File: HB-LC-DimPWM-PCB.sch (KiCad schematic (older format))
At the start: 74 parts, among them J1 SWD, J2 12V Input, J3 Conn_01x04_Male, Q1 S9013, Q10 BSS84, Q11 2N7002, Q12 BSS84, Q13 2N7002, Q14 VS5810AS, Q15 VS5810AS, Q16 VS5810AS, Q2 BSS84, Q3 2N7002, Q4 VS5810AS, Q5 S9013, Q6 S9013, Q7 S9013, Q8 BSS84, Q9 2N7002, U1 STM32F103C8Tx, U2 AMS1117-3.3, Y1 8MHz

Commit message: Add alternate gate driver setup
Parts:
- added C25, C26, C27, C28, C41, C42, C43, C44, C45, C46, C47, C48: 1uF, Capacitor_SMD:C_0402_1005Metric, symbol Device:C
- added C29, C30, C31, C32, C49, C50, C51, C52, C53, C54, C55, C56: 100n, Capacitor_SMD:C_0603_1608Metric, symbol Device:C
- added C33, C34, C35, C36, C57, C58, C59, C60, C61, C62, C63, C64: 100p, Capacitor_SMD:C_0402_1005Metric, symbol Device:C
- added C37, C38, C39, C40, C65, C66, C67, C68, C69, C70, C71, C72: 1uF, Capacitor_SMD:C_0603_1608Metric, symbol Device:C
- added F10, F11, F12, F13, F14, F15, F16, F17, F6, F7, F8, F9: 15V 5A, Fuse:Fuse_2920_7451Metric, symbol Device:Polyfuse
- added J4, J5, J6: Conn_01x04_Male, Connector_Phoenix_MC_HighVoltage:PhoenixContact_MC_1,5_4-G-5.08_1x04_P5.08mm_Horizontal, symbol Connector:Conn_01x04_Male
- added L10, L11, L12, L13, L14, L15, L16, L5, L6, L7, L8, L9: 3.3uH, Inductor_Sunlord:SMD-PIND-10.5x11.5x4_2.5x3.0, symbol Device:L
- added Q17, Q18, Q19, Q20, Q21, Q22, Q23, Q24, Q25, Q26, Q27, Q28: VS5810AS, Package_SO:SOIC-8_3.9x4.9mm_P1.27mm, symbol Transistor_FET:FDS6630A
- added R20, R21, R22, R23, R24, R25, R26, R27, R28, R29, R30, R31: 10k, Resistor_SMD:R_0402_1005Metric, symbol Device:R
- added U10, U11, U12, U13, U14, U3, U4, U5, U6, U7, U8, U9: MCP1416, Package_TO_SOT_SMD:SOT-23-5, symbol Driver_FET:MCP1416
- R14, R15, R16, R17, R18, R19, R6, R7: footprint Resistor_SMD:R_0805_2012Metric -> Resistor_SMD:R_0603_1608Metric; LCSC C17561 -> C23345
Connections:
- wire segments 164 -> 530
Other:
- moved on the sheet: C13, C14, C15, C16, C17, C18, C19, C20, C21, C22, C23, C24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

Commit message: Layout one dimmer channel
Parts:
- removed C25, C26, C27, C28, C41, C42, C43, C44, C45, C46, C47, C48: 1uF, Capacitor_SMD:C_0402_1005Metric, symbol Device:C
- removed C29, C30, C31, C32, C49, C50, C51, C52, C53, C54, C55, C56: 100n, Capacitor_SMD:C_0603_1608Metric, symbol Device:C
- removed C33, C34, C35, C36, C57, C58, C59, C60, C61, C62, C63, C64: 100p, Capacitor_SMD:C_0402_1005Metric, symbol Device:C
- removed C37, C38, C39, C40, C65, C66, C67, C68, C69, C70, C71, C72: 1uF, Capacitor_SMD:C_0603_1608Metric, symbol Device:C
- removed F10, F11, F12, F13, F14, F15, F16, F17, F6, F7, F8, F9: 15V 5A, Fuse:Fuse_2920_7451Metric, symbol Device:Polyfuse
- removed J4, J5, J6: Conn_01x04_Male, Connector_Phoenix_MC_HighVoltage:PhoenixContact_MC_1,5_4-G-5.08_1x04_P5.08mm_Horizontal, symbol Connector:Conn_01x04_Male
- removed L10, L11, L12, L13, L14, L15, L16, L5, L6, L7, L8, L9: 3.3uH, Inductor_Sunlord:SMD-PIND-10.5x11.5x4_2.5x3.0, symbol Device:L
- removed Q17, Q18, Q19, Q20, Q21, Q22, Q23, Q24, Q25, Q26, Q27, Q28: VS5810AS, Package_SO:SOIC-8_3.9x4.9mm_P1.27mm, symbol Transistor_FET:FDS6630A
- removed R20, R21, R22, R23, R24, R25, R26, R27, R28, R29, R30, R31: 10k, Resistor_SMD:R_0402_1005Metric, symbol Device:R
- removed U10, U11, U12, U13, U14, U3, U4, U5, U6, U7, U8, U9: MCP1416, Package_TO_SOT_SMD:SOT-23-5, symbol Driver_FET:MCP1416
- C17, C18, C19, C20: footprint Capacitor_SMD:C_0402_1005Metric -> Capacitor_SMD:C_0805_2012Metric; LCSC C1546 -> C1790
- C21, C22, C23: footprint Capacitor_SMD:C_0603_1608Metric -> Capacitor_SMD:C_1206_3216Metric; LCSC C15849 -> C1848
- C24: footprint Capacitor_SMD:C_0603_1608Metric -> Capacitor_SMD:C_1206_3216Metric
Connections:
- wire segments 530 -> 164

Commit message: Add full layout as PoC
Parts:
- added C25, C26, C27, C28, C37, C38, C39, C40, C41, C42, C43, C44: 1uF, Capacitor_SMD:C_0402_1005Metric, symbol Device:C
- added C29, C30, C31, C32, C45, C46, C47, C48, C49, C50, C51, C52: 100p, Capacitor_SMD:C_0805_2012Metric, symbol Device:C
- added C33, C34, C35, C36, C53, C54, C55, C56, C57, C58, C59, C60: 1uF, Capacitor_SMD:C_1206_3216Metric, symbol Device:C
- added F10, F11, F12, F13, F14, F15, F16, F17, F6, F7, F8, F9: 15V 5A, Fuse:Fuse_2920_7451Metric, symbol Device:Polyfuse
- added J4, J5, J6: Conn_01x04_Male, Connector_Phoenix_MC_HighVoltage:PhoenixContact_MC_1,5_4-G-5.08_1x04_P5.08mm_Horizontal, symbol Connector:Conn_01x04_Male
- added L10, L11, L12, L13, L14, L15, L16, L5, L6, L7, L8, L9: 3.3uH, Inductor_Sunlord:SMD-PIND-10.5x11.5x4_2.5x3.0, symbol Device:L
- added Q17, Q18, Q19, Q20, Q33, Q34, Q35, Q36, Q37, Q38, Q39, Q40: S9013, Package_TO_SOT_SMD:SOT-23, symbol Device:Q_NPN_BEC
- added Q21, Q23, Q25, Q27, Q41, Q43, Q45, Q47, Q49, Q51, Q53, Q55: BSS84, Package_TO_SOT_SMD:SOT-23, symbol Transistor_FET:BSS84
- added Q22, Q24, Q26, Q28, Q42, Q44, Q46, Q48, Q50, Q52, Q54, Q56: 2N7002, Package_TO_SOT_SMD:SOT-23, symbol Transistor_FET:2N7002
- added Q29, Q30, Q31, Q32, Q57, Q58, Q59, Q60, Q61, Q62, Q63, Q64: VS5810AS, Package_SO:SOIC-8_3.9x4.9mm_P1.27mm, symbol Transistor_FET:FDS6630A
- added R20, R21, R22, R23, R36, R37, R38, R39, R40, R41, R42, R43: 10k, Resistor_SMD:R_0402_1005Metric, symbol Device:R
- added R24, R25, R26, R27, R44, R45, R46, R47, R48, R49, R50, R51: 1k, Resistor_SMD:R_0402_1005Metric, symbol Device:R
- added R28, R29, R30, R31, R32, R33, R34, R35, R52, R53, R54, R55, R56, R57, R58, R59, R60, R61, R62, R63, R64, R65, R66, R67: 22R, Resistor_SMD:R_0603_1608Metric, symbol Device:R
- added U3: HomeMatic-sensor, HomeMatic-sensor:HomeMatic-sensor, symbol HomeMatic-sensor:HomeMatic-sensor
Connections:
- net +12V: now also C25.1, C26.1, C27.1, C28.1, C37.1, C38.1, C39.1, C40.1, C41.1, C42.1, C43.1, C44.1, Q21.2 (S), Q23.2 (S), Q25.2 (S), Q27.2 (S), Q41.2 (S), Q43.2 (S), Q45.2 (S), Q47.2 (S), Q49.2 (S), Q51.2 (S), Q53.2 (S), Q55.2 (S), R24.2, R25.2, R26.2, R27.2, R44.2, R45.2, R46.2, R47.2, R48.2, R49.2, R50.2, R51.2
- net GND: now also C25.2, C26.2, C27.2, C28.2, C29.2, C30.2, C31.2, C32.2, C33.2, C34.2, C35.2, C36.2, C37.2, C38.2, C39.2, C40.2, C41.2, C42.2, C43.2, C44.2, C45.2, C46.2, C47.2, C48.2, C49.2, C50.2, C51.2, C52.2, C53.2, C54.2, C55.2, C56.2, C57.2, C58.2, C59.2, C60.2, Q17.2 (E), Q18.2 (E), Q19.2 (E), Q20.2 (E), Q22.2 (S), Q24.2 (S), Q26.2 (S), Q28.2 (S), Q29.1 (S), Q29.2 (S), Q29.3 (S), Q30.1 (S), Q30.2 (S), Q30.3 (S), Q31.1 (S), Q31.2 (S), Q31.3 (S), Q32.1 (S), Q32.2 (S), Q32.3 (S), Q33.2 (E), Q34.2 (E), Q35.2 (E), Q36.2 (E), Q37.2 (E), Q38.2 (E), Q39.2 (E), Q40.2 (E), Q42.2 (S), Q44.2 (S), Q46.2 (S), Q48.2 (S), Q50.2 (S), Q52.2 (S), Q54.2 (S), Q56.2 (S), Q57.1 (S), Q57.2 (S), Q57.3 (S), Q58.1 (S), Q58.2 (S), Q58.3 (S), Q59.1 (S), Q59.2 (S), Q59.3 (S), Q60.1 (S), Q60.2 (S), Q60.3 (S), Q61.1 (S), Q61.2 (S), Q61.3 (S), Q62.1 (S), Q62.2 (S), Q62.3 (S), Q63.1 (S), Q63.2 (S), Q63.3 (S), Q64.1 (S), Q64.2 (S), Q64.3 (S)
- new net: F10.1, J5.1 (Pin_1)
- new net: F11.1, J5.2 (Pin_2)
- new net: F12.1, J5.3 (Pin_3)
- new net: F13.1, J5.4 (Pin_4)
- new net: C53.1, F10.2, L9.2
- new net: C45.1, L9.1, Q57.5 (D), Q57.6 (D), Q57.7 (D), Q57.8 (D)
- new net: Q57.4 (G), R52.2, R53.1
- new net: Q42.3 (D), R53.2
- new net: Q41.3 (D), R52.1
- new net: Q33.3 (C), Q41.1 (G), Q42.1 (G), R44.1
- new net: Q33.1 (B), R36.2
- new net: C54.1, F11.2, L10.2
- new net: C46.1, L10.1, Q58.5 (D), Q58.6 (D), Q58.7 (D), Q58.8 (D)
- new net: Q58.4 (G), R54.2, R55.1
- new net: Q44.3 (D), R55.2
- new net: Q43.3 (D), R54.1
- new net: Q34.3 (C), Q43.1 (G), Q44.1 (G), R45.1
- new net: Q34.1 (B), R37.2
- new net: C55.1, F12.2, L11.2
- new net: C47.1, L11.1, Q59.5 (D), Q59.6 (D), Q59.7 (D), Q59.8 (D)
- new net: Q59.4 (G), R56.2, R57.1
- new net: Q46.3 (D), R57.2
- new net: Q45.3 (D), R56.1
- new net: Q35.3 (C), Q45.1 (G), Q46.1 (G), R46.1
- new net: Q35.1 (B), R38.2
- new net: C56.1, F13.2, L12.2
- new net: C48.1, L12.1, Q60.5 (D), Q60.6 (D), Q60.7 (D), Q60.8 (D)
- new net: Q60.4 (G), R58.2, R59.1
- new net: Q48.3 (D), R59.2
- new net: Q47.3 (D), R58.1
- new net: Q36.3 (C), Q47.1 (G), Q48.1 (G), R47.1
- new net: Q36.1 (B), R39.2
- new net: F6.1, J4.1 (Pin_1)
- new net: F7.1, J4.2 (Pin_2)
- new net: F8.1, J4.3 (Pin_3)
- new net: F9.1, J4.4 (Pin_4)
- new net: C33.1, F6.2, L5.2
- new net: C29.1, L5.1, Q29.5 (D), Q29.6 (D), Q29.7 (D), Q29.8 (D)
- new net: Q29.4 (G), R28.2, R29.1
- new net: Q22.3 (D), R29.2
- new net: Q21.3 (D), R28.1
- new net: Q17.3 (C), Q21.1 (G), Q22.1 (G), R24.1
- new net: Q17.1 (B), R20.2
- new net: C34.1, F7.2, L6.2
- new net: C30.1, L6.1, Q30.5 (D), Q30.6 (D), Q30.7 (D), Q30.8 (D)
- new net: Q30.4 (G), R30.2, R31.1
- new net: Q24.3 (D), R31.2
- new net: Q23.3 (D), R30.1
- new net: Q18.3 (C), Q23.1 (G), Q24.1 (G), R25.1
- new net: Q18.1 (B), R21.2
- new net: C35.1, F8.2, L7.2
- new net: C31.1, L7.1, Q31.5 (D), Q31.6 (D), Q31.7 (D), Q31.8 (D)
- new net: Q31.4 (G), R32.2, R33.1
- new net: Q26.3 (D), R33.2
- new net: Q25.3 (D), R32.1
- new net: Q19.3 (C), Q25.1 (G), Q26.1 (G), R26.1
- new net: Q19.1 (B), R22.2
- new net: C36.1, F9.2, L8.2
- new net: C32.1, L8.1, Q32.5 (D), Q32.6 (D), Q32.7 (D), Q32.8 (D)
- new net: Q32.4 (G), R34.2, R35.1
- new net: Q28.3 (D), R35.2
- new net: Q27.3 (D), R34.1
- new net: Q20.3 (C), Q27.1 (G), Q28.1 (G), R27.1
- new net: Q20.1 (B), R23.2
- new net: F14.1, J6.1 (Pin_1)
- new net: F15.1, J6.2 (Pin_2)
- new net: F16.1, J6.3 (Pin_3)
- new net: F17.1, J6.4 (Pin_4)
- new net: C57.1, F14.2, L13.2
- new net: C49.1, L13.1, Q61.5 (D), Q61.6 (D), Q61.7 (D), Q61.8 (D)
- new net: Q61.4 (G), R60.2, R61.1
- new net: Q50.3 (D), R61.2
- new net: Q49.3 (D), R60.1
- new net: Q37.3 (C), Q49.1 (G), Q50.1 (G), R48.1
- new net: Q37.1 (B), R40.2
- new net: C58.1, F15.2, L14.2
- new net: C50.1, L14.1, Q62.5 (D), Q62.6 (D), Q62.7 (D), Q62.8 (D)
- new net: Q62.4 (G), R62.2, R63.1
- new net: Q52.3 (D), R63.2
- new net: Q51.3 (D), R62.1
- new net: Q38.3 (C), Q51.1 (G), Q52.1 (G), R49.1
- new net: Q38.1 (B), R41.2
- new net: C59.1, F16.2, L15.2
- new net: C51.1, L15.1, Q63.5 (D), Q63.6 (D), Q63.7 (D), Q63.8 (D)
- new net: Q63.4 (G), R64.2, R65.1
- new net: Q54.3 (D), R65.2
- new net: Q53.3 (D), R64.1
- new net: Q39.3 (C), Q53.1 (G), Q54.1 (G), R50.1
- new net: Q39.1 (B), R42.2
- new net: C60.1, F17.2, L16.2
- new net: C52.1, L16.1, Q64.5 (D), Q64.6 (D), Q64.7 (D), Q64.8 (D)
- new net: Q64.4 (G), R66.2, R67.1
- new net: Q56.3 (D), R67.2
- new net: Q55.3 (D), R66.1
- new net: Q40.3 (C), Q55.1 (G), Q56.1 (G), R51.1
- new net: Q40.1 (B), R43.2
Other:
- moved on the sheet: C13, C14, C15, C16, C17, C18, C19, C20, C21, C22, C23, C24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

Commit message: Use hierarchical sheet for dimmer channels
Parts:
- removed C13, C14, C15, C16, C25, C26, C27, C28, C37, C38, C39, C40, C41, C42, C43, C44: 1uF, Capacitor_SMD:C_0402_1005Metric, symbol Device:C
- removed C17, C18, C19, C20, C29, C30, C31, C32, C45, C46, C47, C48, C49, C50, C51, C52: 100p, Capacitor_SMD:C_0805_2012Metric, symbol Device:C
- removed C21, C22, C23, C24, C33, C34, C35, C36, C53, C54, C55, C56, C57, C58, C59, C60: 1uF, Capacitor_SMD:C_1206_3216Metric, symbol Device:C
- removed F10, F11, F12, F13, F14, F15, F16, F17, F2, F3, F4, F5, F6, F7, F8, F9: 15V 5A, Fuse:Fuse_2920_7451Metric, symbol Device:Polyfuse
- removed J3, J4, J5, J6: Conn_01x04_Male, Connector_Phoenix_MC_HighVoltage:PhoenixContact_MC_1,5_4-G-5.08_1x04_P5.08mm_Horizontal, symbol Connector:Conn_01x04_Male
- removed L1, L10, L11, L12, L13, L14, L15, L16, L2, L3, L4, L5, L6, L7, L8, L9: 3.3uH, Inductor_Sunlord:SMD-PIND-10.5x11.5x4_2.5x3.0, symbol Device:L
- removed Q1, Q17, Q18, Q19, Q20, Q33, Q34, Q35, Q36, Q37, Q38, Q39, Q40, Q5, Q6, Q7: S9013, Package_TO_SOT_SMD:SOT-23, symbol Device:Q_NPN_BEC
- removed Q10, Q12, Q2, Q21, Q23, Q25, Q27, Q41, Q43, Q45, Q47, Q49, Q51, Q53, Q55, Q8: BSS84, Package_TO_SOT_SMD:SOT-23, symbol Transistor_FET:BSS84
- removed Q11, Q13, Q22, Q24, Q26, Q28, Q3, Q42, Q44, Q46, Q48, Q50, Q52, Q54, Q56, Q9: 2N7002, Package_TO_SOT_SMD:SOT-23, symbol Transistor_FET:2N7002
- removed Q14, Q15, Q16, Q29, Q30, Q31, Q32, Q4, Q57, Q58, Q59, Q60, Q61, Q62, Q63, Q64: VS5810AS, Package_SO:SOIC-8_3.9x4.9mm_P1.27mm, symbol Transistor_FET:FDS6630A
- removed R10, R20, R21, R22, R23, R36, R37, R38, R39, R4, R40, R41, R42, R43, R8, R9: 10k, Resistor_SMD:R_0402_1005Metric, symbol Device:R
- removed R11, R12, R13, R24, R25, R26, R27, R44, R45, R46, R47, R48, R49, R5, R50, R51: 1k, Resistor_SMD:R_0402_1005Metric, symbol Device:R
- removed R14, R15, R16, R17, R18, R19, R28, R29, R30, R31, R32, R33, R34, R35, R52, R53, R54, R55, R56, R57, R58, R59, R6, R60, R61, R62, R63, R64, R65, R66, R67, R7: 22R, Resistor_SMD:R_0603_1608Metric, symbol Device:R

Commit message: First eight channels finished
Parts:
- added D?: D_Schottky, symbol Device:D_Schottky
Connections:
- net +3V3: now also U3.8 (VDD)
- net GND: now also U3.2 (GND)
- net ~RST: now reaches C1.1, R1.2, U1.7 (NRST)
- net ~RST: now also D?.2 (A)
- net SDA: now reaches U3.3 (SDA)
- net SCL: now reaches U3.4 (SCL)
- net at U3.7 (GPIO): now also D?.1 (K)
- no-connect marks 7 -> 8
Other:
- moved on the sheet: U3
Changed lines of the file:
@@
 	1    0    0    -1
 $EndComp
-Text Label 3750 5050 0    50   ~ 0
+Text Label 4100 5050 2    50   ~ 0
 SWCLK
-Text Label 3750 4950 0    50   ~ 0
+Text Label 4100 4950 2    50   ~ 0
 SWDIO
 NoConn ~ 2450 3450
@@
 L HomeMatic-sensor:HomeMatic-sensor U3
 U 1 1 5E9FF214
-P 5900 8150
-F 0 "U3" H 5900 9131 50  0000 C CNN
-F 1 "HomeMatic-sensor" H 5900 9040 50  0000 C CNN
-F 2 "HomeMatic-sensor:HomeMatic-sensor" H 5900 8150 50  0001 C CNN
-F 3 "" H 5900 8150 50  0001 C CNN
-	1    5900 8150
+P 2050 7200
+F 0 "U3" H 1600 7950 50  0000 C CNN
+F 1 "HomeMatic-sensor" H 2450 7950 50  0000 C CNN
+F 2 "HomeMatic-sensor:HomeMatic-sensor" H 2050 7200 50  0001 C CNN
+F 3 "" H 2050 7200 50  0001 C CNN
+	1    2050 7200
 	1    0    0    -1
 $EndComp
@@
 Wire Wire Line
 	8550 8600 8550 8750
+Text Label 2150 2200 0    50   ~ 0
+~RST
+Wire Wire Line
+	4100 4950 3750 4950
+Wire Wire Line
+	4100 5050 3750 5050
+$Comp
+L power:+3V3 #PWR?
+U 1 1 5EC451F2
+P 2050 6300
+F 0 "#PWR?" H 2050 6150 50  0001 C CNN
+F 1 "+3V3" H 2065 6473 50  0000 C CNN
+F 2 "" H 2050 6300 50  0001 C CNN
+F 3 "" H 2050 6300 50  0001 C CNN
+	1    2050 6300
+	1    0    0    -1
+$EndComp
+Wire Wire Line
+	2050 6300 2050 6400
+$Comp
+L power:GND #PWR?
+U 1 1 5EC474BA
+P 2050 8000
+F 0 "#PWR?" H 2050 7750 50  0001 C CNN
+F 1 "GND" H 2055 7827 50  0000 C CNN
+F 2 "" H 2050 8000 50  0001 C CNN
+F 3 "" H 2050 8000 50  0001 C CNN
+	1    2050 8000
+	1    0    0    -1
+$EndComp
+Wire Wire Line
+	2050 8000 2050 7900
+$Comp
+L Device:D_Schottky D?
+U 1 1 5EC49805
+P 3000 7050
+F 0 "D?" H 3000 7266 50  0000 C CNN
+F 1 "D_Schottky" H 3000 7175 50  0000 C CNN
+F 2 "" H 3000 7050 50  0001 C CNN
+F 3 "~" H 3000 7050 50  0001 C CNN
+	1    3000 7050
+	1    0    0    -1
+$EndComp
+NoConn ~ 2700 6900
+Text Label 3400 7050 2    50   ~ 0
+~RST
+Wire Wire Line
+	3400 7050 3150 7050
+Wire Wire Line
+	2850 7050 2700 7050
+Text Label 1150 6900 0    50   ~ 0
+SDA
+Wire Wire Line
+	1150 6900 1400 6900
+Text Label 1150 7050 0    50   ~ 0
+SCL
+Wire Wire Line
+	1150 7050 1400 7050
 $EndSCHEMATC

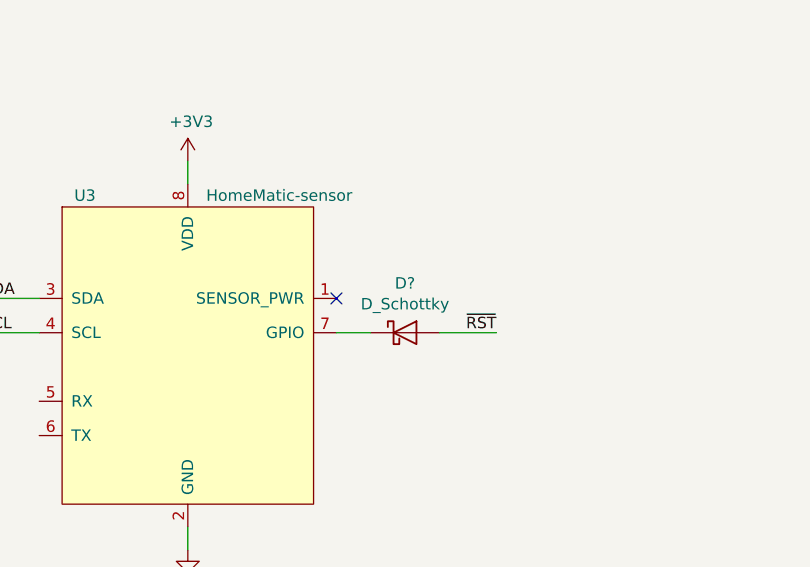
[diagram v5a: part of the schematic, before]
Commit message: Replace 5.08 mm pitch headers by 3.5 mm pitch
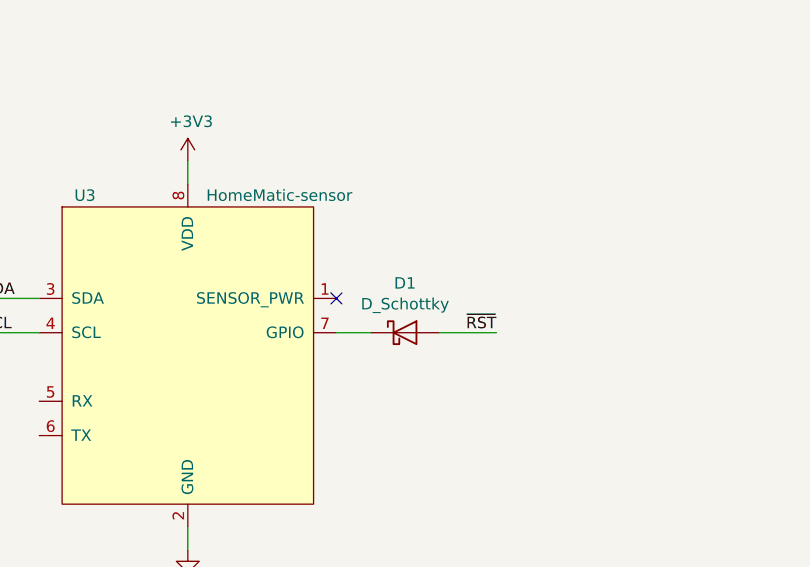
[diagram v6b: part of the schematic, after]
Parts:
- J2: footprint (none) -> Connector_Phoenix_MC_HighVoltage:PhoenixContact_MC_1,5_2-G-5.08_1x02_P5.08mm_Horizontal
- gave numbers to parts that had none: 1
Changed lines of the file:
@@
 F 0 "J2" H 1058 1231 50  0000 C CNN
 F 1 "12V Input" H 1058 1140 50  0000 C CNN
-F 2 "" H 950 1050 50  0001 C CNN
+F 2 "Connector_Phoenix_MC_HighVoltage:PhoenixContact_MC_1,5_2-G-5.08_1x02_P5.08mm_Horizontal" H 950 1050 50  0001 C CNN
 F 3 "~" H 950 1050 50  0001 C CNN
 	1    950  1050
@@
 	4100 5050 3750 5050
 $Comp
-L power:+3V3 #PWR?
+L power:+3V3 #PWR0121
 U 1 1 5EC451F2
 P 2050 6300
-F 0 "#PWR?" H 2050 6150 50  0001 C CNN
+F 0 "#PWR0121" H 2050 6150 50  0001 C CNN
 F 1 "+3V3" H 2065 6473 50  0000 C CNN
 F 2 "" H 2050 6300 50  0001 C CNN
@@
 	2050 6300 2050 6400
 $Comp
-L power:GND #PWR?
+L power:GND #PWR0122
 U 1 1 5EC474BA
 P 2050 8000
-F 0 "#PWR?" H 2050 7750 50  0001 C CNN
+F 0 "#PWR0122" H 2050 7750 50  0001 C CNN
 F 1 "GND" H 2055 7827 50  0000 C CNN
 F 2 "" H 2050 8000 50  0001 C CNN
@@
 	2050 8000 2050 7900
 $Comp
-L Device:D_Schottky D?
+L Device:D_Schottky D1
 U 1 1 5EC49805
 P 3000 7050
-F 0 "D?" H 3000 7266 50  0000 C CNN
+F 0 "D1" H 3000 7266 50  0000 C CNN
 F 1 "D_Schottky" H 3000 7175 50  0000 C CNN
 F 2 "" H 3000 7050 50  0001 C CNN

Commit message: Layout board
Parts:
- added F18, F19: 500mA, Fuse:Fuse_2512_6332Metric, symbol Device:Fuse
- D1: footprint (none) -> Diode_SMD:D_SOD-123; LCSC (none) -> C8598
- J2: footprint Connector_Phoenix_MC_HighVoltage:PhoenixContact_MC_1,5_2-G-5.08_1x02_P5.08mm_Horizontal -> Connector_Wago_714:Wago_714-162_1x02_P3.50mm_Horizontal
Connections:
- net +12V: now also F1.2, J2.1 (Pin_1), F18.2, F19.2; no longer C10.1, C8.1, C9.1, F1.1, U2.3 (VI)
- net SCL: now also U1.21 (PB10)
- net SDA: now also U1.22 (PB11)
- net PWM4: now reaches U1.10 (PA0)
- net PWM5: now reaches U1.11 (PA1)
- net PWM6: now reaches U1.12 (PA2)
- net PWM7: now reaches U1.13 (PA3)
- net PWM8: now reaches U1.16 (PA6)
- net PWM9: now reaches U1.17 (PA7)
- net PWM10: now reaches U1.18 (PB0)
- net PWM11: now reaches U1.19 (PB1)
- net PWM0: now reaches U1.29 (PA8)
- net PWM1: now reaches U1.30 (PA9)
- net PWM2: now reaches U1.31 (PA10)
- net PWM3: now reaches U1.32 (PA11)
- net PWM12: now reaches U1.42 (PB6)
- net PWM13: now reaches U1.43 (PB7)
- net PWM14: now reaches U1.45 (PB8)
- net PWM15: now reaches U1.46 (PB9)
- new net: C10.1, C8.1, C9.1, F1.1, U2.3 (VI)
- new net Dimmer channel 1/+12V: F18.1
- new net Dimmer channel 3/+12V: F19.1
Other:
- moved on the sheet: C10, C11, C12, C8, C9, D1, F1, J2, U2, U3

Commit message: Add additional bypassing
Add 4x 10uF to gate driver supplies
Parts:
- added C61, C62, C63, C64: 10uF, Capacitor_SMD:C_1206_3216Metric, symbol Device:C
- C8: value 220uF -> 100uF; footprint Capacitor_SMD:CP_Elec_8x10 -> Capacitor_SMD:CP_Elec_8x6.7
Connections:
- net Dimmer channel 1/+12V: now also C61.1, C63.1
- net Dimmer channel 3/+12V: now also C62.1, C64.1
- net GND: now also C61.2, C62.2, C63.2, C64.2
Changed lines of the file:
@@
 P 2000 1450
 F 0 "C8" H 2118 1496 50  0000 L CNN
-F 1 "220uF" H 2118 1405 50  0000 L CNN
-F 2 "Capacitor_SMD:CP_Elec_8x10" H 2038 1300 50  0001 C CNN
-F 3 "~" H 2000 1450 50  0001 C CNN
+F 1 "100uF" H 2118 1405 50  0000 L CNN
+F 2 "Capacitor_SMD:CP_Elec_8x6.7" H 2038 1300 50  0001 C CNN
+F 3 "C311668" H 2000 1450 50  0001 C CNN
 F 4 "C127967" H 2000 1450 50  0001 C CNN "LCSC"
 	1    2000 1450
@@
 Wire Wire Line
 	9350 4400 9350 4700
+$Comp
+L Device:C C64
+U 1 1 5EEACB05
+P 9150 4700
+F 0 "C64" V 8898 4700 50  0000 C CNN
+F 1 "10uF" V 8989 4700 50  0000 C CNN
+F 2 "Capacitor_SMD:C_1206_3216Metric" H 9188 4550 50  0001 C CNN
+F 3 "~" H 9150 4700 50  0001 C CNN
+F 4 "C13585" V 9150 4700 50  0001 C CNN "LCSC"
+	1    9150 4700
+	0    1    1    0
+$EndComp
+Wire Wire Line
+	9300 4700 9350 4700
+Connection ~ 9350 4700
+$Comp
+L power:GND #PWR0129
+U 1 1 5EEB1AE2
+P 8900 4800
+F 0 "#PWR0129" H 8900 4550 50  0001 C CNN
+F 1 "GND" H 8905 4627 50  0000 C CNN
+F 2 "" H 8900 4800 50  0001 C CNN
+F 3 "" H 8900 4800 50  0001 C CNN
+	1    8900 4800
+	1    0    0    -1
+$EndComp
+Wire Wire Line
+	8900 4800 8900 4700
+Wire Wire Line
+	8900 4700 9000 4700
+$Comp
+L Device:C C62
+U 1 1 5EEB68A5
+P 7400 4750
+F 0 "C62" V 7148 4750 50  0000 C CNN
+F 1 "10uF" V 7239 4750 50  0000 C CNN
+F 2 "Capacitor_SMD:C_1206_3216Metric" H 7438 4600 50  0001 C CNN
+F 3 "~" H 7400 4750 50  0001 C CNN
+F 4 "C13585" V 7400 4750 50  0001 C CNN "LCSC"
+	1    7400 4750
+	0    1    1    0
+$EndComp
+Wire Wire Line
+	7550 4750 7600 4750
+$Comp
+L power:GND #PWR0130
+U 1 1 5EEB68AC
+P 7150 4850
+F 0 "#PWR0130" H 7150 4600 50  0001 C CNN
+F 1 "GND" H 7155 4677 50  0000 C CNN
+F 2 "" H 7150 4850 50  0001 C CNN
+F 3 "" H 7150 4850 50  0001 C CNN
+	1    7150 4850
+	1    0    0    -1
+$EndComp
+Wire Wire Line
+	7150 4850 7150 4750
+Wire Wire Line
+	7150 4750 7250 4750
+Connection ~ 7600 4750
+$Comp
+L Device:C C61
+U 1 1 5EEBBB5F
+P 7400 1650
+F 0 "C61" V 7148 1650 50  0000 C CNN
+F 1 "10uF" V 7239 1650 50  0000 C CNN
+F 2 "Capacitor_SMD:C_1206_3216Metric" H 7438 1500 50  0001 C CNN
+F 3 "~" H 7400 1650 50  0001 C CNN
+F 4 "C13585" V 7400 1650 50  0001 C CNN "LCSC"
+	1    7400 1650
+	0    1    1    0
+$EndComp
+Wire Wire Line
+	7550 1650 7600 1650
+$Comp
+L power:GND #PWR0131
+U 1 1 5EEBBB66
+P 7150 1750
+F 0 "#PWR0131" H 7150 1500 50  0001 C CNN
+F 1 "GND" H 7155 1577 50  0000 C CNN
+F 2 "" H 7150 1750 50  0001 C CNN
+F 3 "" H 7150 1750 50  0001 C CNN
+	1    7150 1750
+	1    0    0    -1
+$EndComp
+Wire Wire Line
+	7150 1750 7150 1650
+Wire Wire Line
+	7150 1650 7250 1650
+Connection ~ 7600 1650
+$Comp
+L Device:C C63
+U 1 1 5EEC0E3B
+P 9150 1550
+F 0 "C63" V 8898 1550 50  0000 C CNN
+F 1 "10uF" V 8989 1550 50  0000 C CNN
+F 2 "Capacitor_SMD:C_1206_3216Metric" H 9188 1400 50  0001 C CNN
+F 3 "~" H 9150 1550 50  0001 C CNN
+F 4 "C13585" V 9150 1550 50  0001 C CNN "LCSC"
+	1    9150 1550
+	0    1    1    0
+$EndComp
+Wire Wire Line
+	9300 1550 9350 1550
+$Comp
+L power:GND #PWR0132
+U 1 1 5EEC0E42
+P 8900 1650
+F 0 "#PWR0132" H 8900 1400 50  0001 C CNN
+F 1 "GND" H 8905 1477 50  0000 C CNN
+F 2 "" H 8900 1650 50  0001 C CNN
+F 3 "" H 8900 1650 50  0001 C CNN
+	1    8900 1650
+	1    0    0    -1
+$EndComp
+Wire Wire Line
+	8900 1650 8900 1550
+Wire Wire Line
+	8900 1550 9000 1550
+Connection ~ 9350 1550
 $EndSCHEMATC
